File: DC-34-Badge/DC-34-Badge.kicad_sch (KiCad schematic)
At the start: 36 parts, among them U1 ESP32-S3-MINI-1, U2 AP2112K-3.3

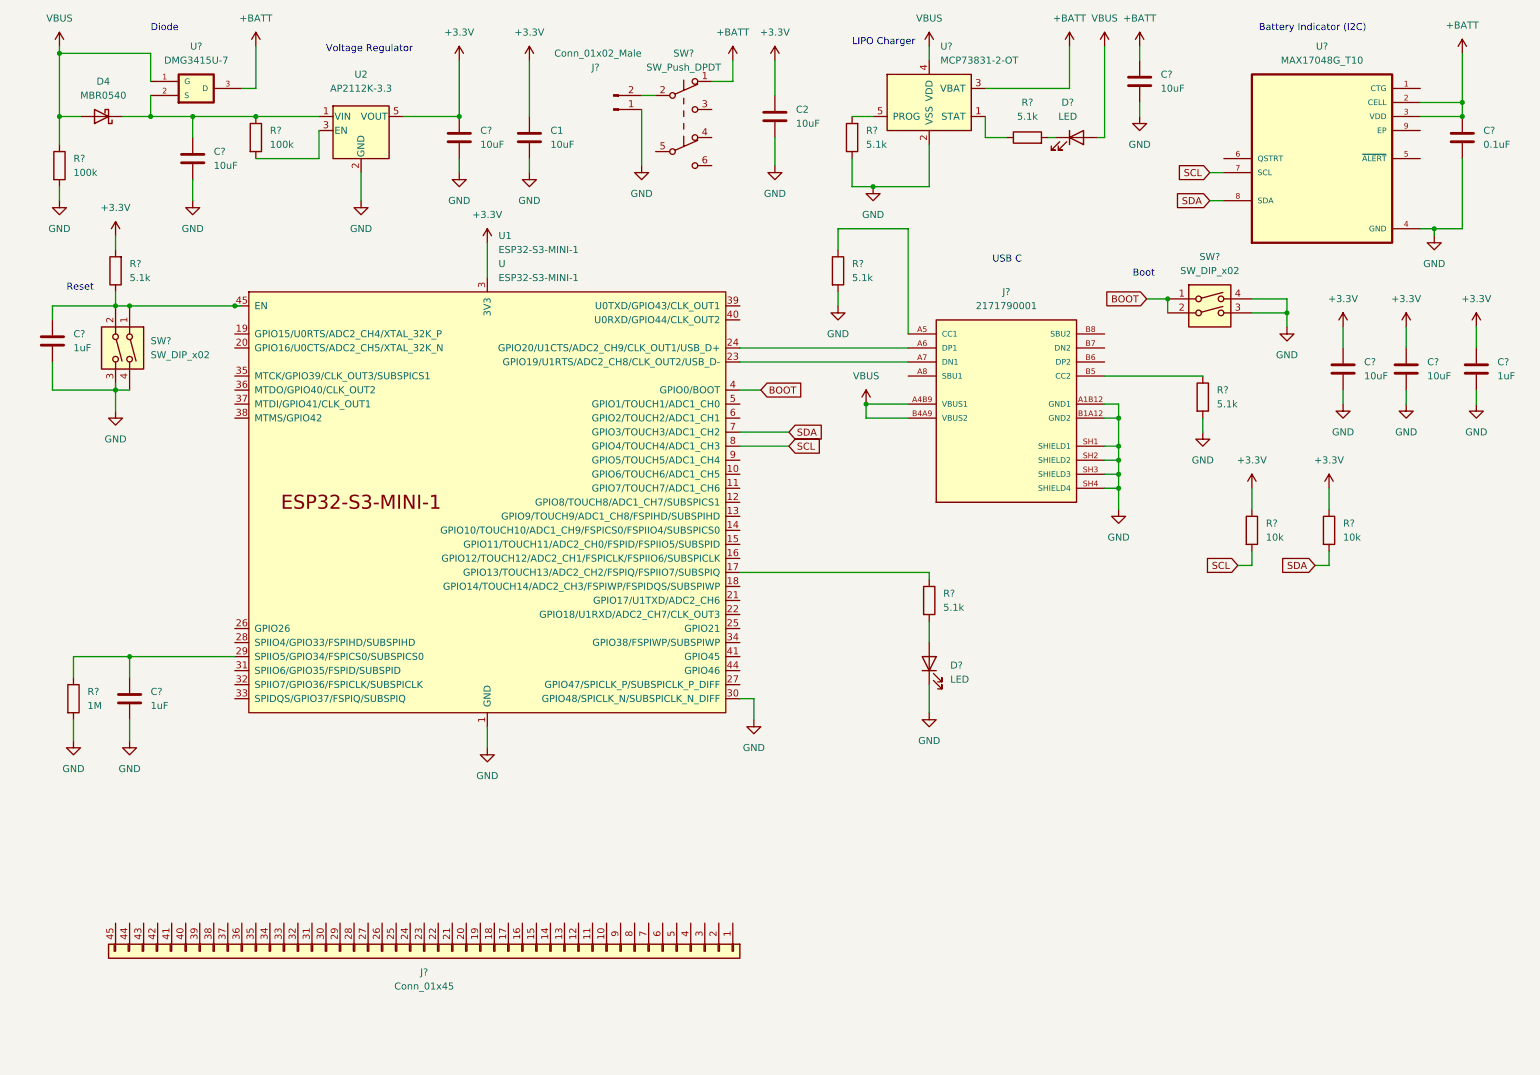
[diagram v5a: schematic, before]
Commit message: Buttons and Screen Added
Added buttons and screen and hooked up to design.
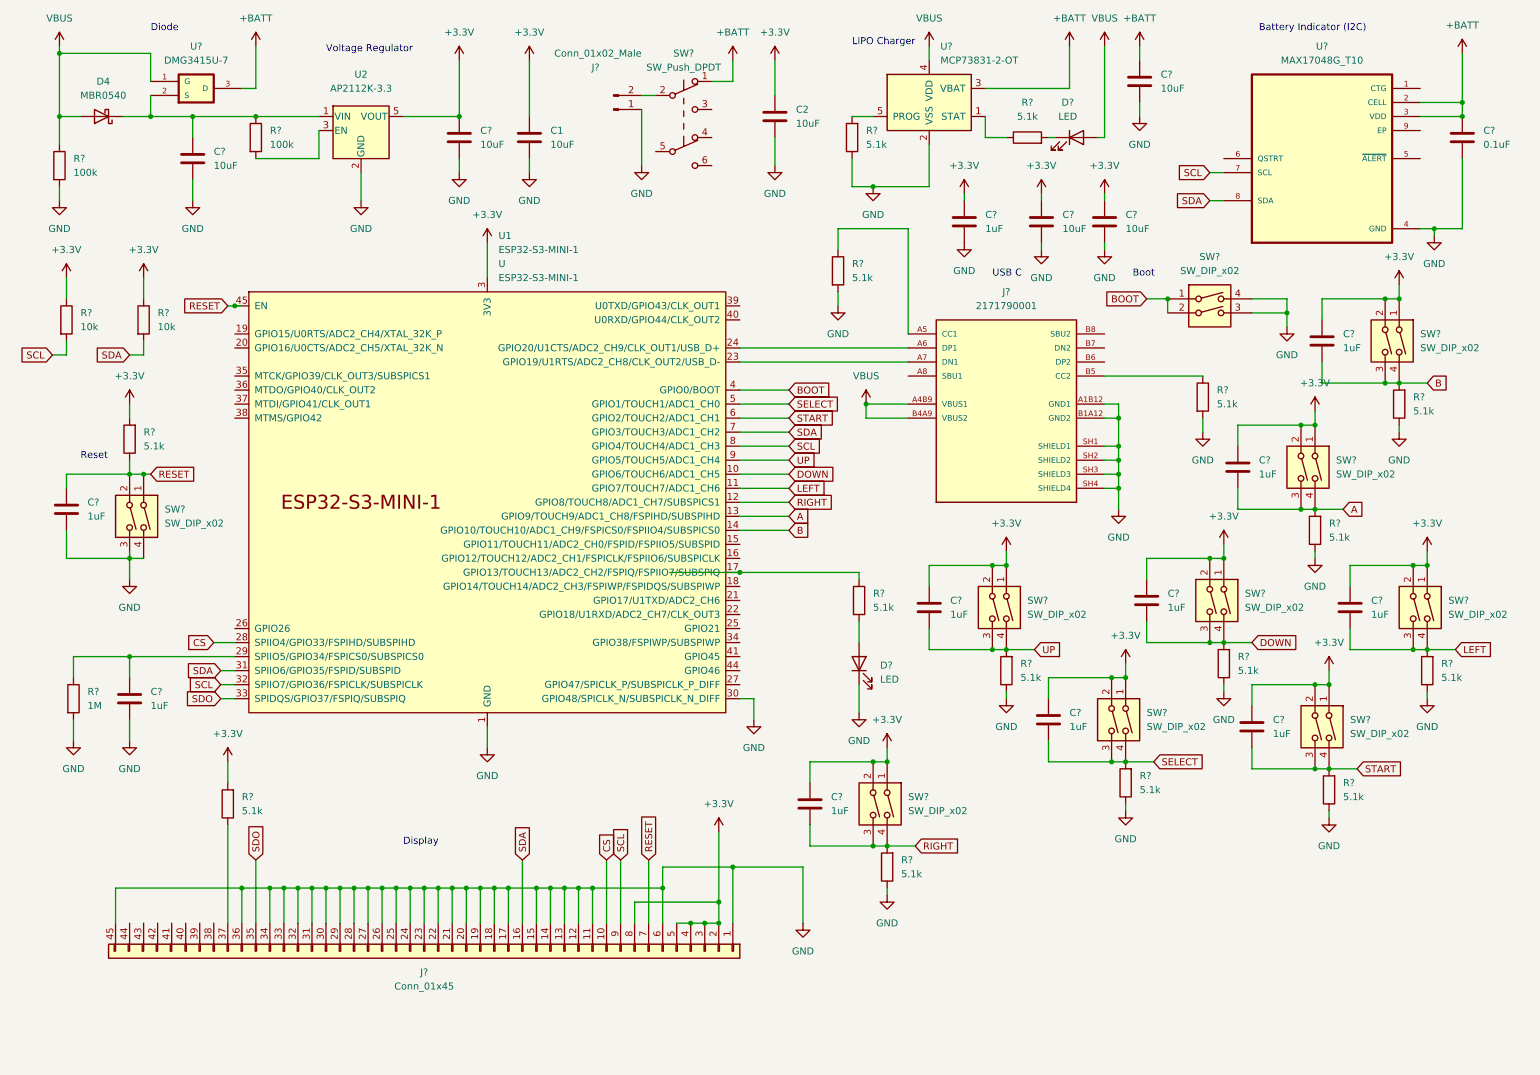
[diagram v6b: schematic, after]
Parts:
- added C? (x8): 1uF, Capacitor_SMD:C_0402_1005Metric, symbol Device:C
- added R? (x9): 5.1k, Resistor_SMD:R_0402_1005Metric, symbol Device:R
- added SW? (x8): SW_DIP_x02, Button_Switch_THT:SW_PUSH_6mm, symbol Switch:SW_DIP_x02
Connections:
- net +3.3V: now also J?.2 (Pin_2), J?.3 (Pin_3), J?.4 (Pin_4), J?.5 (Pin_5), J?.8 (Pin_8), C?.1, C?.1, C?.1, C?.1, C?.1, C?.1, C?.1, C?.1, R?.2, SW?.1, SW?.1, SW?.1, SW?.1, SW?.1, SW?.1, SW?.1, SW?.1, SW?.2, SW?.2, SW?.2, SW?.2, SW?.2, SW?.2, SW?.2, SW?.2
- net GND: now also J?.1 (Pin_1), J?.11 (Pin_11), J?.12 (Pin_12), J?.13 (Pin_13), J?.14 (Pin_14), J?.15 (Pin_15), J?.17 (Pin_17), J?.18 (Pin_18), J?.19 (Pin_19), J?.20 (Pin_20), J?.21 (Pin_21), J?.22 (Pin_22), J?.23 (Pin_23), J?.24 (Pin_24), J?.25 (Pin_25), J?.26 (Pin_26), J?.27 (Pin_27), J?.28 (Pin_28), J?.29 (Pin_29), J?.30 (Pin_30), J?.31 (Pin_31), J?.32 (Pin_32), J?.33 (Pin_33), J?.34 (Pin_34), J?.36 (Pin_36), J?.45 (Pin_45), J?.6 (Pin_6), R?.1, R?.1, R?.1, R?.1, R?.1, R?.1, R?.1, R?.1
- net SCL: now also J?.9 (Pin_9), U1.32 (SPIIO7/GPIO36/FSPICLK/SUBSPICLK)
- net SDA: now also J?.16 (Pin_16), U1.31 (SPIIO6/GPIO35/FSPID/SUBSPID)
- net RESET: now reaches C?.1, R?.1, SW?.1, SW?.2, U1.45 (EN)
- net RESET: now also J?.7 (Pin_7)
- net CS: now reaches J?.10 (Pin_10)
- net CS: now also U1.28 (SPIIO4/GPIO33/FSPIHD/SUBSPIHD)
- net SDO: now reaches J?.35 (Pin_35)
- net SDO: now also U1.33 (SPIDQS/GPIO37/FSPIQ/SUBSPIQ)
- net at J?.37 (Pin_37): now also R?.1
- net DOWN: now reaches U1.10 (GPIO6/TOUCH6/ADC1_CH5)
- net DOWN: now also C?.2, R?.2, SW?.3, SW?.4
- net LEFT: now reaches U1.11 (GPIO7/TOUCH7/ADC1_CH6)
- net LEFT: now also C?.2, R?.2, SW?.3, SW?.4
- net RIGHT: now reaches U1.12 (GPIO8/TOUCH8/ADC1_CH7/SUBSPICS1)
- net RIGHT: now also C?.2, R?.2, SW?.3, SW?.4
- net A: now reaches U1.13 (GPIO9/TOUCH9/ADC1_CH8/FSPIHD/SUBSPIHD)
- net A: now also C?.2, R?.2, SW?.3, SW?.4
- net B: now reaches U1.14 (GPIO10/TOUCH10/ADC1_CH9/FSPICS0/FSPIIO4/SUBSPICS0)
- net B: now also C?.2, R?.2, SW?.3, SW?.4
- net SELECT: now reaches U1.5 (GPIO1/TOUCH1/ADC1_CH0)
- net SELECT: now also C?.2, R?.2, SW?.3, SW?.4
- net START: now reaches U1.6 (GPIO2/TOUCH2/ADC1_CH1)
- net START: now also C?.2, R?.2, SW?.3, SW?.4
- net UP: now reaches U1.9 (GPIO5/TOUCH5/ADC1_CH4)
- net UP: now also C?.2, R?.2, SW?.3, SW?.4
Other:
- note added: "Display"
- moved on the sheet: C?, D?, R?, SW?

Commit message: Added Rumble
Added H-Bridge to enable motor control from ESP-32.
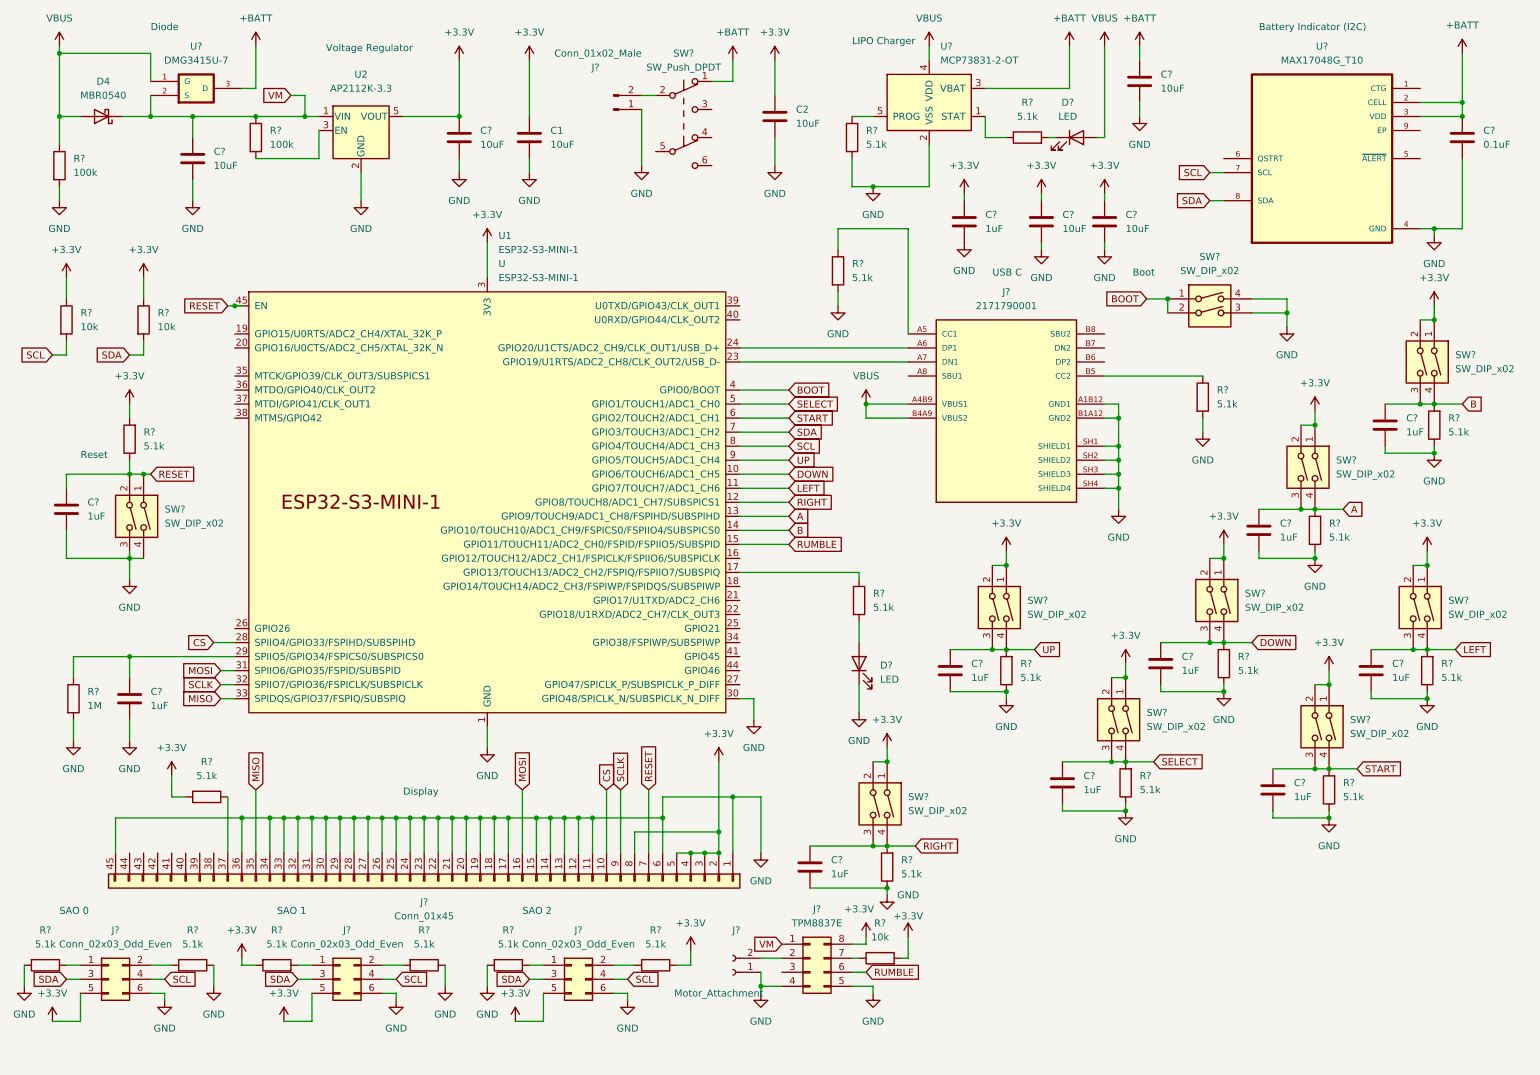
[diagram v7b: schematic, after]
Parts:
- added J? (x3): Conn_02x03_Odd_Even, Connector_PinHeader_2.54mm:PinHeader_2x03_P2.54mm_Vertical, symbol Connector_Generic:Conn_02x03_Odd_Even
- added J?: TPM8837E, Package_DFN_QFN:DFN-8-1EP_2x2mm_P0.5mm_EP0.8x1.6mm, symbol Connector_Generic:Conn_02x04_Counter_Clockwise
- added J?: Motor_Attachment, Connector_Wire:SolderWire-0.1sqmm_1x02_P3.6mm_D0.4mm_OD1mm, symbol Connector:Conn_01x02_Female
- added R? (x6): 5.1k, Resistor_SMD:R_0402_1005Metric, symbol Device:R
- added R?: 10k, Resistor_SMD:R_0402_1005Metric, symbol Device:R
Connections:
- net +3.3V: now also J?.5 (Pin_5), J?.5 (Pin_5), J?.5 (Pin_5), J?.8 (Pin_8), R?.1, R?.2, R?.2; no longer C?.1, C?.1, C?.1, C?.1, C?.1, C?.1, C?.1, C?.1
- net A: now also C?.1; no longer C?.2
- net B: now also C?.1; no longer C?.2
- net DOWN: now also C?.1; no longer C?.2
- net GND: now also C?.2, C?.2, C?.2, C?.2, C?.2, C?.2, C?.2, C?.2, J?.1 (Pin_1), J?.4 (Pin_4), J?.5 (Pin_5), J?.6 (Pin_6), J?.6 (Pin_6), J?.6 (Pin_6), R?.1, R?.1, R?.2, R?.2
- net LEFT: now also C?.1; no longer C?.2
- net RIGHT: now also C?.1; no longer C?.2
- net SCL: now also J?.4 (Pin_4), J?.4 (Pin_4), J?.4 (Pin_4); no longer J?.9 (Pin_9), U1.32 (SPIIO7/GPIO36/FSPICLK/SUBSPICLK)
- net SDA: now also J?.3 (Pin_3), J?.3 (Pin_3), J?.3 (Pin_3); no longer J?.16 (Pin_16), U1.31 (SPIIO6/GPIO35/FSPID/SUBSPID)
- net SELECT: now also C?.1; no longer C?.2
- net START: now also C?.1; no longer C?.2
- net UP: now also C?.1; no longer C?.2
- net VM: now reaches C?.1, D4.1 (K), R?.1, U2.1 (VIN), U?.2 (S)
- net VM: now also J?.1 (Pin_1)
- net RUMBLE: now reaches U1.15 (GPIO11/TOUCH11/ADC2_CH0/FSPID/FSPIIO5/SUBSPID)
- net RUMBLE: now also J?.6 (Pin_6)
- net SDO renamed MISO
- new net: J?.1 (Pin_1), R?.1 (x3)
- new net: J?.2 (Pin_2), R?.2 (x3)
- new net: J?.2 (Pin_2), J?.2 (Pin_2)
- new net: J?.7 (Pin_7), R?.1
- new net MOSI: J?.16 (Pin_16), U1.31 (SPIIO6/GPIO35/FSPID/SUBSPID)
- new net SCLK: J?.9 (Pin_9), U1.32 (SPIIO7/GPIO36/FSPICLK/SUBSPICLK)
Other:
- note added: "SAO 0"
- note added: "SAO 1"
- note added: "SAO 2"
- moved on the sheet: C?, J?, R?, SW?

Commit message: Added display circuit, buzzer circuit, and rearranged componets.
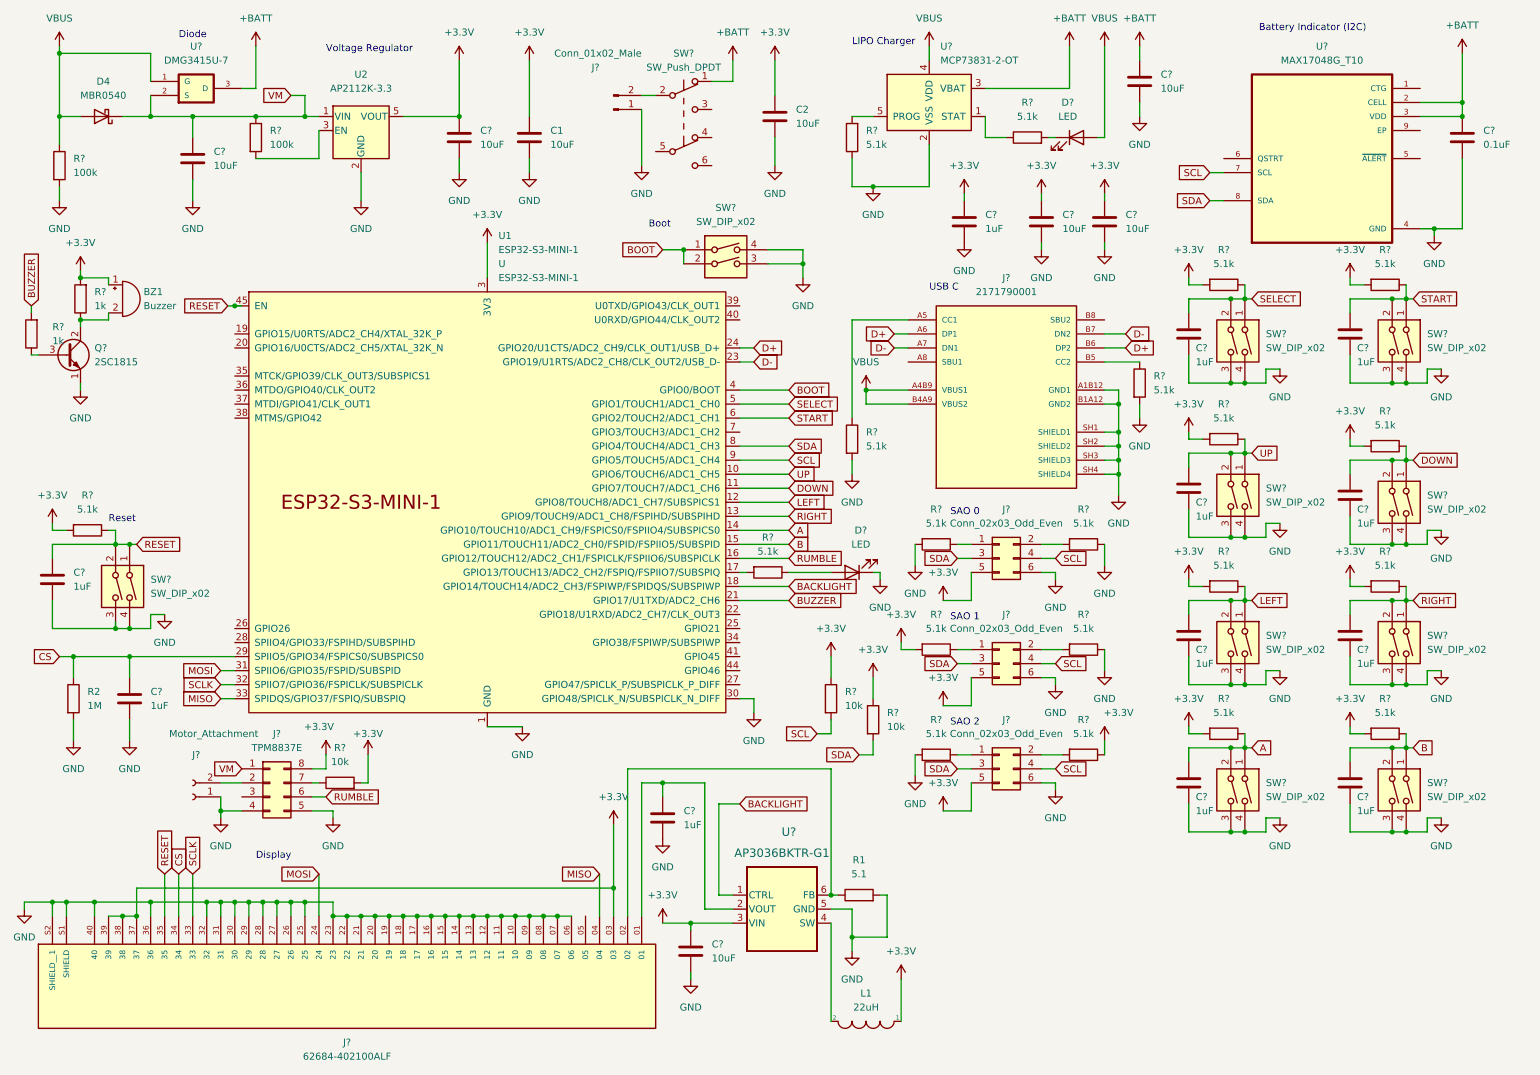
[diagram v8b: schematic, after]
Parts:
- removed C? (x8): 1uF, Capacitor_SMD:C_0402_1005Metric, symbol Device:C
- removed J?: Conn_01x45, CF4245FH0R0:ZIF_45_0.5mm, symbol ZIF:Conn_01x45
- removed R? (x9): 5.1k, Resistor_SMD:R_0402_1005Metric, symbol Device:R
- removed SW? (x8): SW_DIP_x02, Button_Switch_THT:SW_PUSH_6mm, symbol Switch:SW_DIP_x02
- added BZ1: Buzzer, Diode_THT:D_A-405_P5.08mm_Vertical_AnodeUp, symbol Device:Buzzer
- added C? (x9): 1uF, Capacitor_SMD:C_0402_1005Metric, symbol Device:C
- added C?: 10uF, Capacitor_SMD:C_0402_1005Metric, symbol Device:C
- added J?: 62684-402100ALF, 62684-402100ALF:AMPHENOL_62684-402100ALF, symbol 62684-402100ALF:62684-402100ALF
- added L1: 22uH, Inductor_SMD:L_1210_3225Metric, symbol pspice:INDUCTOR
- added Q?: 2SC1815, Package_TO_SOT_SMD:SOT-23, symbol Transistor_BJT:2SC1815
- added R1: 5.1, Resistor_SMD:R_0402_1005Metric, symbol Device:R
- added R? (x2): 1k, Resistor_SMD:R_0402_1005Metric, symbol Device:R
- added R? (x8): 5.1k, Resistor_SMD:R_0402_1005Metric, symbol Device:R
- added SW? (x8): SW_DIP_x02, Button_Switch_THT:SW_PUSH_6mm, symbol Switch:SW_DIP_x02
- added U?: AP3036BKTR-G1, SOIC6_AP3036BKTR-G1_DIO, symbol 2026-04-03_03-59-32:AP3036BKTR-G1
- gave numbers to parts that had none: 1
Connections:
- net +3.3V: now also BZ1.1 (-), C?.1, J?.03, J?.37, J?.38, J?.39, L1.1, R?.2, R?.2, R?.2, R?.2, R?.2, R?.2, R?.2, R?.2, R?.2, U?.3 (VIN)
- net A: now also U1.14 (GPIO10/TOUCH10/ADC1_CH9/FSPICS0/FSPIIO4/SUBSPICS0), C?.1, R?.1, SW?.1, SW?.2; no longer U1.13 (GPIO9/TOUCH9/ADC1_CH8/FSPIHD/SUBSPIHD)
- net B: now also U1.15 (GPIO11/TOUCH11/ADC2_CH0/FSPID/FSPIIO5/SUBSPID), C?.1, R?.1, SW?.1, SW?.2; no longer U1.14 (GPIO10/TOUCH10/ADC1_CH9/FSPICS0/FSPIIO4/SUBSPICS0)
- net CS: now also C?.1, R2.1, U1.29 (SPIIO5/GPIO34/FSPICS0/SUBSPICS0), J?.34; no longer U1.28 (SPIIO4/GPIO33/FSPIHD/SUBSPIHD)
- net DOWN: now also U1.11 (GPIO7/TOUCH7/ADC1_CH6), C?.1, R?.1, SW?.1, SW?.2; no longer U1.10 (GPIO6/TOUCH6/ADC1_CH5)
- net GND: now also C?.2, C?.2, C?.2, C?.2, C?.2, C?.2, C?.2, C?.2, C?.2, C?.2, J?.06, J?.07, J?.08, J?.09, J?.10, J?.11, J?.12, J?.13, J?.14, J?.15, J?.16, J?.17, J?.18, J?.19, J?.20, J?.21, J?.22, J?.23, J?.25, J?.26, J?.27, J?.28, J?.29, J?.30, J?.31, J?.32, J?.36, J?.40, J?.S1 (SHIELD), J?.S2 (SHIELD__1), Q?.1 (E), R1.2, SW?.3, SW?.3, SW?.3, SW?.3, SW?.3, SW?.3, SW?.3, SW?.3, SW?.4, SW?.4, SW?.4, SW?.4, SW?.4, SW?.4, SW?.4, SW?.4, U?.5 (GND)
- net LEFT: now also U1.12 (GPIO8/TOUCH8/ADC1_CH7/SUBSPICS1), C?.1, R?.1, SW?.1, SW?.2; no longer U1.11 (GPIO7/TOUCH7/ADC1_CH6)
- net MISO: now also J?.04
- net MOSI: now also J?.24
- net RESET: now also J?.35
- net RIGHT: now also U1.13 (GPIO9/TOUCH9/ADC1_CH8/FSPIHD/SUBSPIHD), C?.1, R?.1, SW?.1, SW?.2; no longer U1.12 (GPIO8/TOUCH8/ADC1_CH7/SUBSPICS1)
- net RUMBLE: now also U1.16 (GPIO12/TOUCH12/ADC2_CH1/FSPICLK/FSPIIO6/SUBSPICLK); no longer U1.15 (GPIO11/TOUCH11/ADC2_CH0/FSPID/FSPIIO5/SUBSPID)
- net SCL: now also U1.9 (GPIO5/TOUCH5/ADC1_CH4); no longer U1.8 (GPIO4/TOUCH4/ADC1_CH3)
- net SCLK: now also J?.33
- net SDA: now also U1.8 (GPIO4/TOUCH4/ADC1_CH3); no longer U1.7 (GPIO3/TOUCH3/ADC1_CH2)
- net SELECT: now also C?.1, R?.1, SW?.1, SW?.2
- net START: now also C?.1, R?.1, SW?.1, SW?.2
- net UP: now also U1.10 (GPIO6/TOUCH6/ADC1_CH5), C?.1, R?.1, SW?.1, SW?.2; no longer U1.9 (GPIO5/TOUCH5/ADC1_CH4)
- net at U1.17 (GPIO13/TOUCH13/ADC2_CH2/FSPIQ/FSPIIO7/SUBSPIQ): now also R?.2; no longer R?.1
- net BACKLIGHT: now reaches U1.18 (GPIO14/TOUCH14/ADC2_CH3/FSPIWP/FSPIDQS/SUBSPIWP)
- net BACKLIGHT: now also U?.1 (CTRL)
- net BUZZER: now reaches U1.21 (GPIO17/U1TXD/ADC2_CH6)
- net BUZZER: now also R?.2
- net D-: now reaches J?.A7 (DN1), U1.23 (GPIO19/U1RTS/ADC2_CH8/CLK_OUT2/USB_D-)
- net D-: now also J?.B7 (DN2)
- net D+: now reaches J?.A6 (DP1), U1.24 (GPIO20/U1CTS/ADC2_CH9/CLK_OUT1/USB_D+)
- net D+: now also J?.B6 (DP2)
- net at D?.2 (A): now also R?.1; no longer R?.2
- new net: C?.1, J?.01, U?.2 (VOUT)
- new net: J?.02, R1.1, U?.6 (FB)
- new net: BZ1.2 (+), Q?.2 (C), R?.1
- new net: Q?.3 (B), R?.1
- new net: L1.2, U?.4 (SW)
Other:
- moved on the sheet: C?, D?, J?, R?, SW?
